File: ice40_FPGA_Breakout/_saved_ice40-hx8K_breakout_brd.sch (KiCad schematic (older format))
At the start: 0 parts

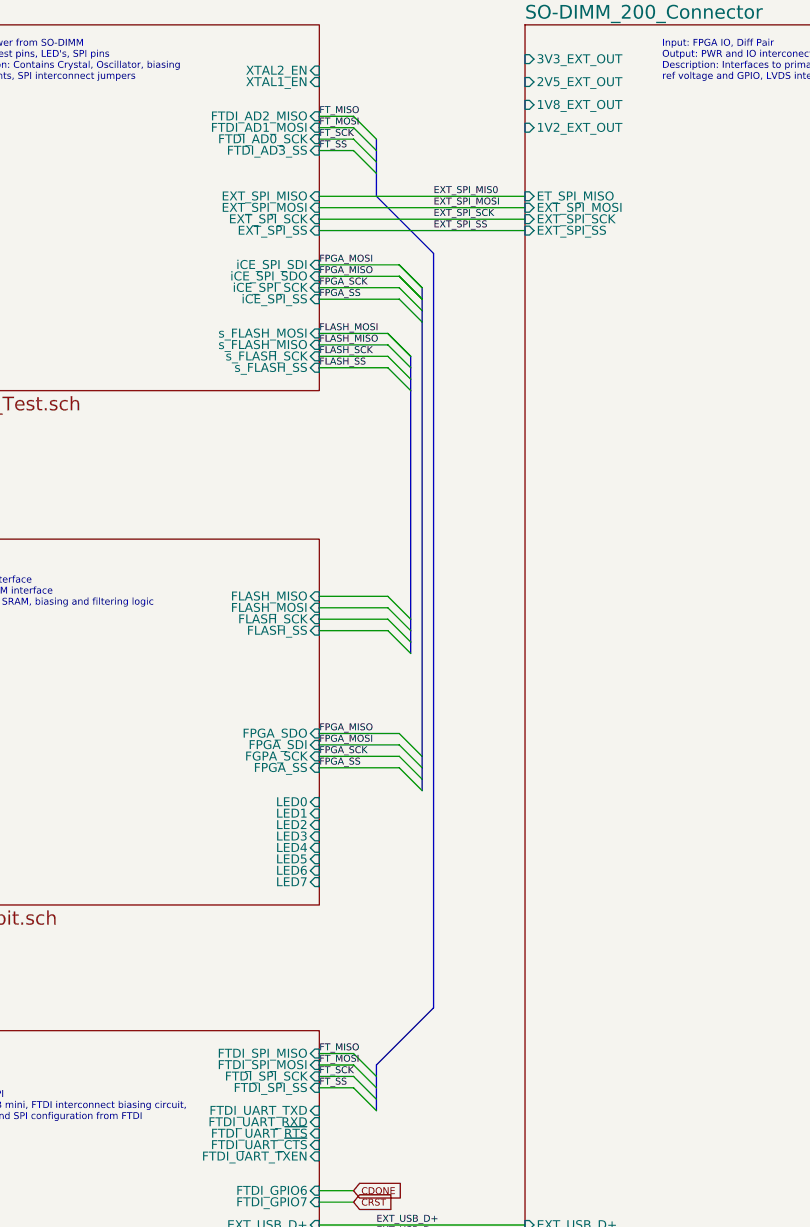
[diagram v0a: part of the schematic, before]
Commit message: global nets changed to hierarchy net, interconnects updated
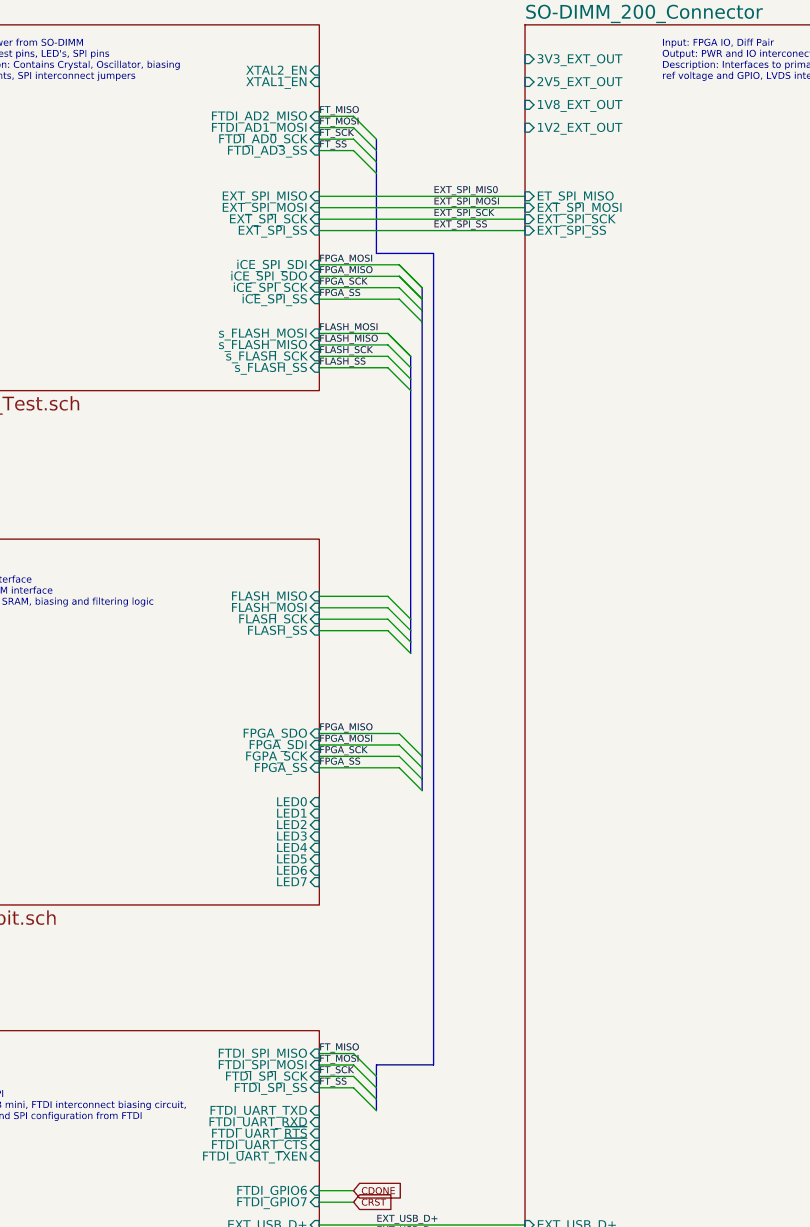
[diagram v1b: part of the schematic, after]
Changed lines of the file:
@@
 	3950 1550 3950 1600
 Wire Bus Line
-	3950 1600 3950 1650
+	3950 1600 3950 1900
 Wire Bus Line
-	3950 1650 3950 1750
+	3950 1900 3950 2000
 Wire Bus Line
 	3950 5550 3950 5600
@@
 	3700 1550 3850 1550
 Wire Bus Line
-	3950 1750 4200 2000
+	3950 2000 4200 2000
 Wire Bus Line
-	4200 2000 4200 5300
+	4200 2000 4200 5550
 Wire Bus Line
-	4200 5300 3950 5550
+	4200 5550 3950 5550
 Wire Bus Line
 	4150 2150 4150 2150
